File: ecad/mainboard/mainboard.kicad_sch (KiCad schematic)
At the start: 20 parts, among them J1 Dot Matrix Side A, J2 Dot Matrix Side B, J3 Dot Matrix Side A, J4 Dot Matrix Side B, J5 Conn_01x08_Socket, J6 Conn_01x08_Socket, J7 USB_C_Receptacle_PowerOnly_6P, J8 Conn_01x08_Socket, J9 Conn_01x08_Socket, SW1 Left Button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

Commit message: complete schematics for v1 of board
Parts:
- removed J7: USB_C_Receptacle_PowerOnly_6P, symbol Connector:USB_C_Receptacle_PowerOnly_6P
- added R10, R11, R12, R13, R14, R15, R16, R9: ${dm_resistor}, symbol Device:R_US
- added R17: 10k, symbol Device:R_US
- added R18, R19: 4.7k, symbol Device:R_US
- added U1: PCF8575DBR, Package_SO:SSOP-24_5.3x8.2mm_P0.65mm, symbol Interface_Expansion:PCF8575DBR
- J5: value Conn_01x08_Socket -> ESP32C3 Super Mini Left
- J6: value Conn_01x08_Socket -> ESP32C3 Super Mini Right
- J8: value Conn_01x08_Socket -> IO Expander Module - Left
- J9: value Conn_01x08_Socket -> IO Expander Module - Right
- R1, R2, R3, R4, R5, R6, R7, R8: value 330 -> ${dm_resistor}
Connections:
- net GPIO10 is gone; now on net BUZZ: J5.6 (Pin_6)
- net DM_A1: now also R1.1
- net DM_A2: now also R2.1
- net DM_A3: now also R3.1
- net DM_A4: now also R4.1
- net DM_A5: now also R5.1
- net DM_A6: now also R6.1
- net DM_A7: now also R7.1
- net DM_A8: now also R8.1
- net DM_B1: now also R9.1
- net DM_B2: now also R10.1
- net DM_B3: now also R11.1
- net DM_B4: now also R12.1
- net DM_B5: now also R13.1
- net DM_B6: now also R14.1
- net DM_B7: now also R15.1
- net DM_B8: now also R16.1
- net GND: now also U1.12 (GND), U1.2 (A1), U1.21 (A0), U1.3 (A2)
- net LEFT_BTN: now also J6.8 (Pin_8)
- net RIGHT_BTN: now also J6.7 (Pin_7)
- net SCL: now also R19.2, U1.22 (SCL)
- net SDA: now also R18.2, U1.23 (SDA)
- net P5: now reaches R6.2
- net P5: now also J8.6 (Pin_6), U1.9 (P5)
- net P4: now reaches R5.2
- net P4: now also J8.5 (Pin_5), U1.8 (P4)
- net P1: now reaches R2.2
- net P1: now also J8.2 (Pin_2), U1.5 (P1)
- net P0: now reaches R1.2
- net P0: now also J8.1 (Pin_1), U1.4 (P0)
- net P3: now reaches R4.2
- net P3: now also J8.4 (Pin_4), U1.7 (P3)
- net P7: now reaches R8.2
- net P7: now also J8.8 (Pin_8), U1.11 (P7)
- net P2: now reaches R3.2
- net P2: now also J8.3 (Pin_3), U1.6 (P2)
- net P6: now reaches J8.7 (Pin_7)
- net P6: now also R7.2, U1.10 (P6)
- net P10: now reaches J9.1 (Pin_1)
- net P10: now also R9.2, U1.13 (P10)
- net P11: now reaches J9.2 (Pin_2)
- net P11: now also R10.2, U1.14 (P11)
- net P12: now reaches J9.3 (Pin_3)
- net P12: now also R11.2, U1.15 (P12)
- net P13: now reaches J9.4 (Pin_4)
- net P13: now also R12.2, U1.16 (P13)
- net P14: now reaches J9.5 (Pin_5)
- net P14: now also R13.2, U1.17 (P14)
- net P15: now reaches J9.6 (Pin_6)
- net P15: now also R14.2, U1.18 (P15)
- net P16: now reaches J9.7 (Pin_7)
- net P16: now also R15.2, U1.19 (P16)
- net P17: now reaches J9.8 (Pin_8)
- net P17: now also R16.2, U1.20 (P17)
- net +5V: no longer names the net of J6.1 (Pin_1)
- net GPIO20: no longer names the net of J5.7 (Pin_7)
- net GPIO21: no longer names the net of J5.8 (Pin_8)
- removed net GPIO5: J5.1 (Pin_1), J6.3 (Pin_3), J6.4 (Pin_4), J6.5 (Pin_5), J6.6 (Pin_6), J6.7 (Pin_7), J6.8 (Pin_8)
- net GPIO6: no longer names the net of J5.2 (Pin_2)
- net GPIO7: no longer names the net of J5.3 (Pin_3)
- new net +3.3V: J6.3 (Pin_3), R17.1, R18.1, R19.1, U1.24 (VCC)
- new net ~{INT}: J6.5 (Pin_5), R17.2, U1.1 (~{INT})
- no-connect marks 0 -> 8
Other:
- moved on the sheet: BZ1, J1, J2, J3, J4, J5, J6, J8, J9, R1, R2, R3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

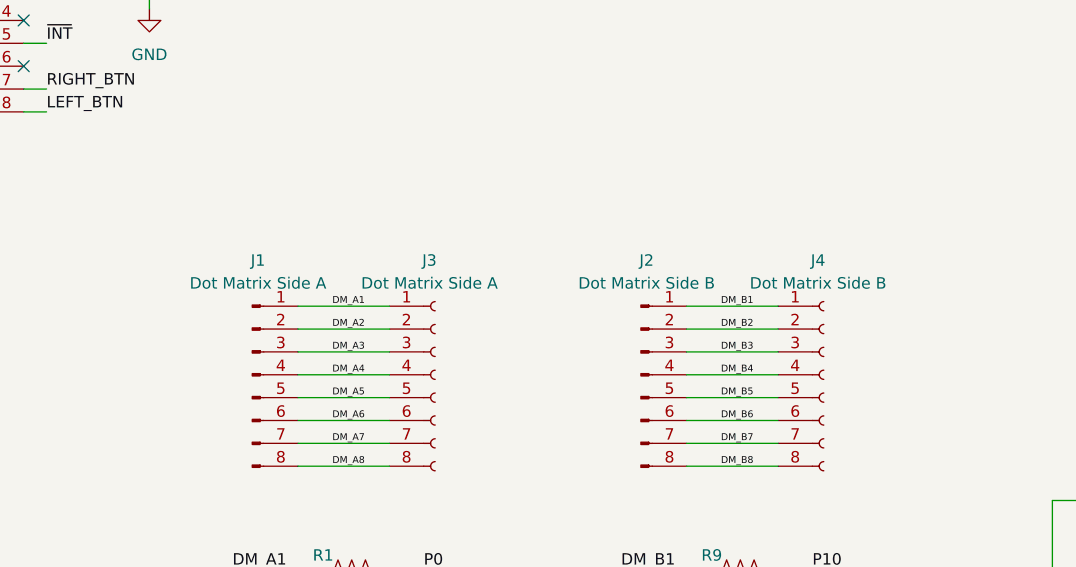
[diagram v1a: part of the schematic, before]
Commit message: update footprints for the schematic
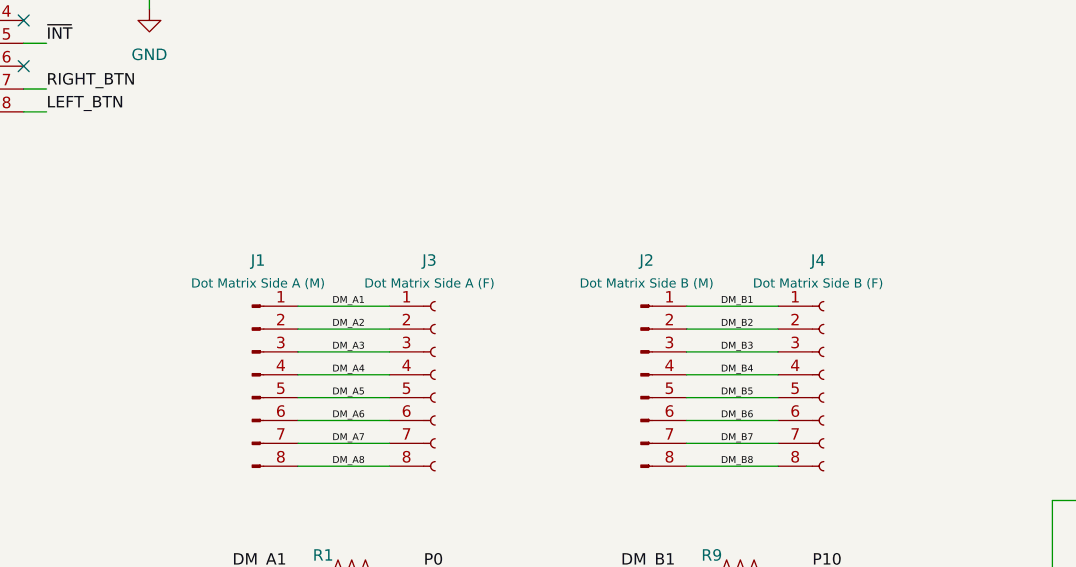
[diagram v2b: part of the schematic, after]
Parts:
- BZ1: footprint (none) -> Buzzer_Beeper:Buzzer_12x9.5RM7.6
- J1: value Dot Matrix Side A -> Dot Matrix Side A (M); footprint (none) -> Connector_PinHeader_2.54mm:PinHeader_1x08_P2.54mm_Vertical
- J2: value Dot Matrix Side B -> Dot Matrix Side B (M); footprint (none) -> Connector_PinHeader_2.54mm:PinHeader_1x08_P2.54mm_Vertical
- J3: value Dot Matrix Side A -> Dot Matrix Side A (F); footprint (none) -> Connector_PinSocket_2.54mm:PinSocket_1x08_P2.54mm_Vertical
- J4: value Dot Matrix Side B -> Dot Matrix Side B (F); footprint (none) -> Connector_PinSocket_2.54mm:PinSocket_1x08_P2.54mm_Vertical
- J5, J6, J8, J9: footprint (none) -> Connector_PinSocket_2.54mm:PinSocket_1x08_P2.54mm_Vertical
- R1, R10, R11, R12, R13, R14, R15, R16, R17, R18, R19, R2, R3, R4, R5, R6, R7, R8, R9: footprint (none) -> Resistor_SMD:R_0805_2012Metric
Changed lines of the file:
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@@
 			)
 		)
-		(property "Footprint" ""
+		(property "Footprint" "Resistor_SMD:R_0805_2012Metric"
 			(at 100.584 127.254 90)
 			(hide yes)
@@
 			)
 		)
-		(property "Value" "Dot Matrix Side B"
+		(property "Value" "Dot Matrix Side B (F)"
 			(at 151.765 64.77 0)
 			(show_name no)
@@
 			(effects
 				(font
-					(size 1.27 1.27)
+					(size 1.016 1.016)
 				)
 			)
 		)
-		(property "Footprint" ""
+		(property "Footprint" "Connector_PinSocket_2.54mm:PinSocket_1x08_P2.54mm_Vertical"
 			(at 152.4 74.93 0)
 			(hide yes)
@@
 			)
 		)
-		(property "Value" "Dot Matrix Side B"
+		(property "Value" "Dot Matrix Side B (M)"
 			(at 132.715 64.77 0)
 			(show_name no)
@@
 			(effects
 				(font
-					(size 1.27 1.27)
+					(size 1.016 1.016)
 				)
 			)
 		)
-		(property "Footprint" ""
+		(property "Footprint" "Connector_PinHeader_2.54mm:PinHeader_1x08_P2.54mm_Vertical"
 			(at 132.08 74.93 0)
 			(hide yes)
@@
 			)
 		)
-		(property "Footprint" ""
+		(property "Footprint" "Resistor_SMD:R_0805_2012Metric"
 			(at 100.584 120.904 90)
 			(hide yes)
@@
 			)
 		)
-		(property "Value" "Dot Matrix Side A"
+		(property "Value" "Dot Matrix Side A (F)"
 			(at 108.585 64.77 0)
 			(show_name no)
@@
 			(effects
 				(font
-					(size 1.27 1.27)
+					(size 1.016 1.016)
 				)
 			)
 		)
-		(property "Footprint" ""
+		(property "Footprint" "Connector_PinSocket_2.54mm:PinSocket_1x08_P2.54mm_Vertical"
 			(at 109.22 74.93 0)
 			(hide yes)
@@
 			)
 		)
-		(property "Footprint" ""
+		(property "Footprint" "Resistor_SMD:R_0805_2012Metric"
 			(at 143.764 141.224 90)
 			(hide yes)
@@
 			)
 		)
-		(property "Footprint" ""
+		(property "Footprint" "Resistor_SMD:R_0805_2012Metric"
 			(at 27.686 98.044 90)
 			(hide yes)
@@
 			)
 		)
-		(property "Footprint" ""
+		(property "Footprint" "Resistor_SMD:R_0805_2012Metric"
 			(at 143.764 114.554 90)
 			(hide yes)
@@
 			)
 		)
-		(property "Footprint" ""
+		(property "Footprint" "Resistor_SMD:R_0805_2012Metric"
 			(at 100.584 101.854 90)
 			(hide yes)
@@
 			)
 		)
-		(property "Footprint" ""
+		(property "Footprint" "Resistor_SMD:R_0805_2012Metric"
 			(at 100.584 95.504 90)
 			(hide yes)
@@
 			)
 		)
-		(property "Footprint" ""
+		(property "Footprint" "Resistor_SMD:R_0805_2012Metric"
 			(at 100.584 114.554 90)
 			(hide yes)
@@
 			)
 		)
-		(property "Footprint" ""
+		(property "Footprint" "Connector_PinSocket_2.54mm:PinSocket_1x08_P2.54mm_Vertical"
 			(at 27.94 35.56 0)
 			(hide yes)
@@
 			)
 		)
-		(property "Footprint" ""
+		(property "Footprint" "Resistor_SMD:R_0805_2012Metric"
 			(at 100.584 141.224 90)
 			(hide yes)
@@
 			)
 		)
-		(property "Footprint" ""
+		(property "Footprint" "Resistor_SMD:R_0805_2012Metric"
 			(at 143.764 133.604 90)
 			(hide yes)
@@
 			)
 		)
-		(property "Footprint" ""
+		(property "Footprint" "Resistor_SMD:R_0805_2012Metric"
 			(at 100.584 108.204 90)
 			(hide yes)
@@
 			)
 		)
-		(property "Value" "Dot Matrix Side A"
+		(property "Value" "Dot Matrix Side A (M)"
 			(at 89.535 64.77 0)
 			(show_name no)
@@
 			(effects
 				(font
-					(size 1.27 1.27)
+					(size 1.016 1.016)
 				)
 			)
 		)
-		(property "Footprint" ""
+		(property "Footprint" "Connector_PinHeader_2.54mm:PinHeader_1x08_P2.54mm_Vertical"
 			(at 88.9 74.93 0)
 			(hide yes)
@@
 			)
 		)
-		(property "Footprint" ""
+		(property "Footprint" "Resistor_SMD:R_0805_2012Metric"
 			(at 143.764 95.504 90)
 			(hide yes)
@@
 			)
 		)
-		(property "Footprint" ""
+		(property "Footprint" "Resistor_SMD:R_0805_2012Metric"
 			(at 39.116 98.044 90)
 			(hide yes)
@@
 			)
 		)
-		(property "Footprint" ""
+		(property "Footprint" "Connector_PinSocket_2.54mm:PinSocket_1x08_P2.54mm_Vertical"
 			(at 224.79 59.69 0)
 			(hide yes)
@@
 			)
 		)
-		(property "Footprint" ""
+		(property "Footprint" "Resistor_SMD:R_0805_2012Metric"
 			(at 143.764 108.204 90)
 			(hide yes)
@@
 			)
 		)
-		(property "Footprint" ""
+		(property "Footprint" "Resistor_SMD:R_0805_2012Metric"
 			(at 143.764 120.904 90)
 			(hide yes)
@@
 			)
 		)
-		(property "Footprint" ""
+		(property "Footprint" "Buzzer_Beeper:Buzzer_12x9.5RM7.6"
 			(at 26.035 170.18 90)
 			(hide yes)
@@
 			)
 		)
-		(property "Footprint" ""
+		(property "Footprint" "Connector_PinSocket_2.54mm:PinSocket_1x08_P2.54mm_Vertical"
 			(at 58.42 35.56 0)
 			(hide yes)
@@
 			)
 		)
-		(property "Footprint" ""
+		(property "Footprint" "Resistor_SMD:R_0805_2012Metric"
 			(at 178.816 108.204 90)
 			(hide yes)
@@
 			)
 		)
-		(property "Footprint" ""
+		(property "Footprint" "Resistor_SMD:R_0805_2012Metric"
 			(at 143.764 101.854 90)
 			(hide yes)
@@
 			)
 		)
-		(property "Footprint" ""
+		(property "Footprint" "Resistor_SMD:R_0805_2012Metric"
 			(at 100.584 133.604 90)
 			(hide yes)
@@
 			)
 		)
-		(property "Footprint" ""
+		(property "Footprint" "Resistor_SMD:R_0805_2012Metric"
 			(at 143.764 127.254 90)
 			(hide yes)
@@
 			)
 		)
-		(property "Footprint" ""
+		(property "Footprint" "Connector_PinSocket_2.54mm:PinSocket_1x08_P2.54mm_Vertical"
 			(at 260.35 59.69 0)
 			(hide yes)

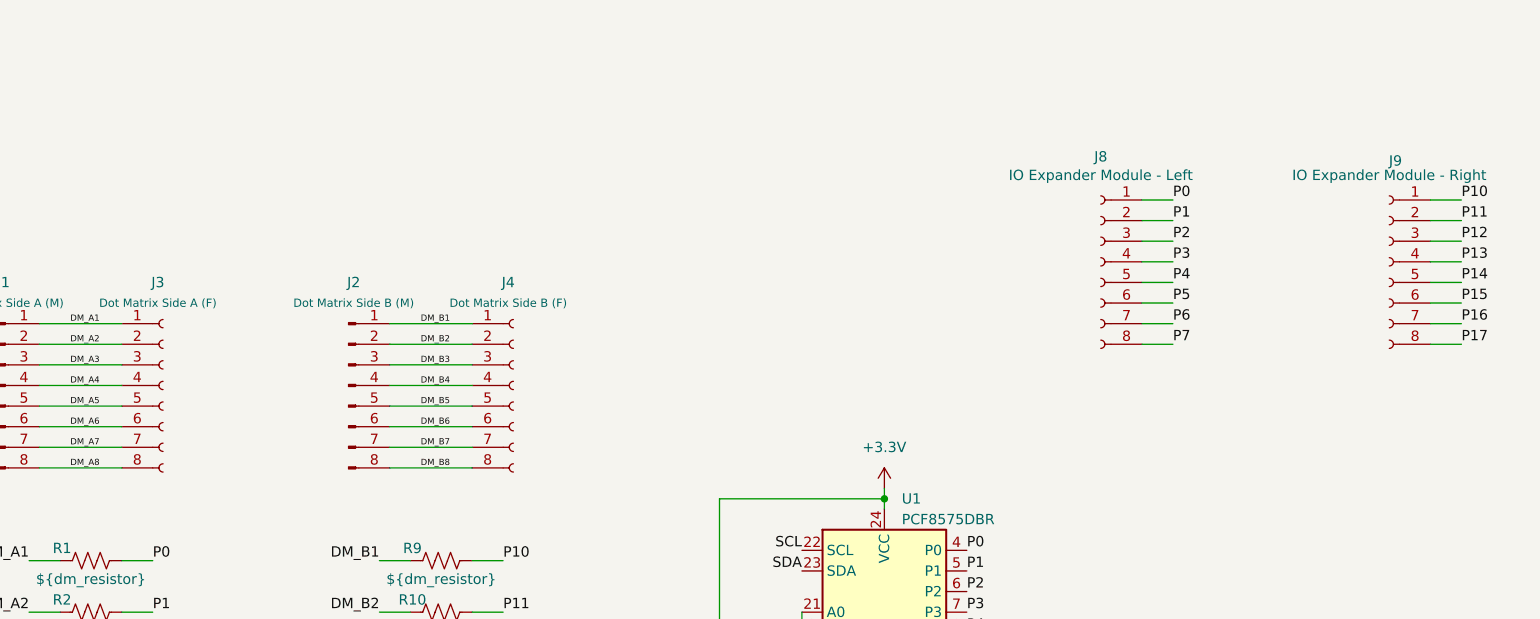
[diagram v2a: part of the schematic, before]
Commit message: update pin headers for dot matrix
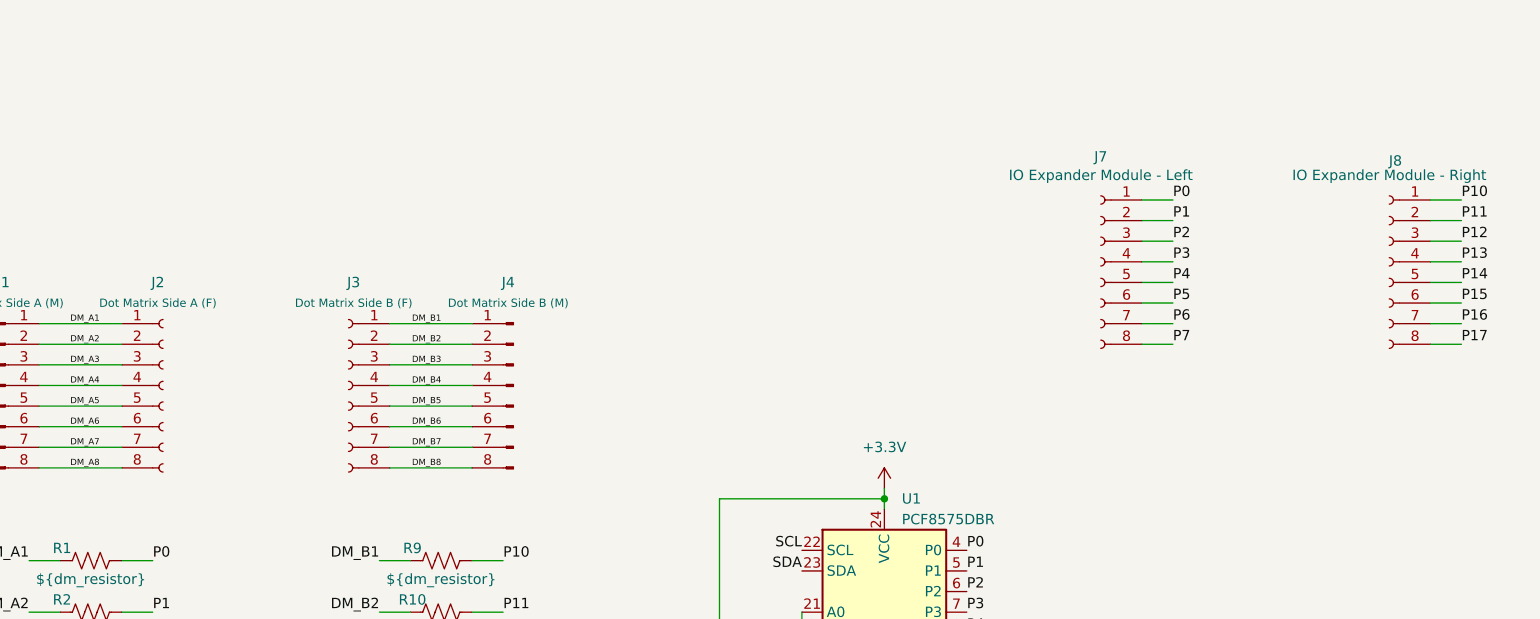
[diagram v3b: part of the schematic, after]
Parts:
- renumbered J3 to J2, J4 to J3, J2 to J4, J8 to J7, J9 to J8
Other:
- moved on the sheet: J3, J4
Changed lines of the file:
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@@
 	(wire
 		(pts
-			(xy 137.16 67.31) (xy 147.32 67.31)
+			(xy 147.32 67.31) (xy 137.16 67.31)
 		)
 		(stroke
@@
 	(wire
 		(pts
-			(xy 137.16 74.93) (xy 147.32 74.93)
+			(xy 147.32 74.93) (xy 137.16 74.93)
 		)
 		(stroke
@@
 	(wire
 		(pts
-			(xy 137.16 77.47) (xy 147.32 77.47)
+			(xy 147.32 77.47) (xy 137.16 77.47)
 		)
 		(stroke
@@
 	(wire
 		(pts
-			(xy 137.16 85.09) (xy 147.32 85.09)
+			(xy 147.32 85.09) (xy 137.16 85.09)
 		)
 		(stroke
@@
 	(wire
 		(pts
-			(xy 137.16 82.55) (xy 147.32 82.55)
+			(xy 147.32 82.55) (xy 137.16 82.55)
 		)
 		(stroke
@@
 	(wire
 		(pts
-			(xy 137.16 72.39) (xy 147.32 72.39)
+			(xy 147.32 72.39) (xy 137.16 72.39)
 		)
 		(stroke
@@
 	(wire
 		(pts
-			(xy 137.16 69.85) (xy 147.32 69.85)
+			(xy 147.32 69.85) (xy 137.16 69.85)
 		)
 		(stroke
@@
 	(wire
 		(pts
-			(xy 137.16 80.01) (xy 147.32 80.01)
+			(xy 147.32 80.01) (xy 137.16 80.01)
 		)
 		(stroke
@@
 	)
 	(label "DM_B2"
-		(at 140.97 69.85 0)
+		(at 143.51 69.85 180)
 		(effects
 			(font
 				(size 0.762 0.762)
 			)
-			(justify left bottom)
+			(justify right bottom)
 		)
 	)
@@
 	)
 	(label "DM_B6"
-		(at 140.97 80.01 0)
+		(at 143.51 80.01 180)
 		(effects
 			(font
 				(size 0.762 0.762)
 			)
-			(justify left bottom)
+			(justify right bottom)
 		)
 	)
 	(label "DM_B8"
-		(at 140.97 85.09 0)
+		(at 143.51 85.09 180)
 		(effects
 			(font
 				(size 0.762 0.762)
 			)
-			(justify left bottom)
+			(justify right bottom)
 		)
 	)
@@
 	)
 	(label "DM_B3"
-		(at 140.97 72.39 0)
+		(at 143.51 72.39 180)
 		(effects
 			(font
 				(size 0.762 0.762)
 			)
-			(justify left bottom)
+			(justify right bottom)
 		)
 	)
@@
 	)
 	(label "DM_B4"
-		(at 140.97 74.93 0)
+		(at 143.51 74.93 180)
 		(effects
 			(font
 				(size 0.762 0.762)
 			)
-			(justify left bottom)
+			(justify right bottom)
 		)
 	)
@@
 	)
 	(label "DM_B1"
-		(at 140.97 67.31 0)
+		(at 143.51 67.31 180)
 		(effects
 			(font
 				(size 0.762 0.762)
 			)
-			(justify left bottom)
+			(justify right bottom)
 		)
 	)
@@
 	)
 	(label "DM_B7"
-		(at 140.97 82.55 0)
+		(at 143.51 82.55 180)
 		(effects
 			(font
 				(size 0.762 0.762)
 			)
-			(justify left bottom)
+			(justify right bottom)
 		)
 	)
@@
 	)
 	(label "DM_B5"
-		(at 140.97 77.47 0)
+		(at 143.51 77.47 180)
 		(effects
 			(font
 				(size 0.762 0.762)
 			)
-			(justify left bottom)
+			(justify right bottom)
 		)
 	)
@@
 	(symbol
 		(lib_id "Connector:Conn_01x08_Socket")
-		(at 152.4 74.93 0)
+		(at 132.08 74.93 0)
+		(mirror y)
 		(unit 1)
 		(body_style 1)
@@
 		(in_pos_files yes)
 		(dnp no)
-		(property "Reference" "J4"
-			(at 151.765 62.23 0)
+		(property "Reference" "J3"
+			(at 132.715 62.23 0)
 			(show_name no)
 			(do_not_autoplace no)
@@
 		)
 		(property "Value" "Dot Matrix Side B (F)"
-			(at 151.765 64.77 0)
+			(at 132.715 64.77 0)
 			(show_name no)
 			(do_not_autoplace no)
@@
 		)
 		(property "Footprint" "Connector_PinSocket_2.54mm:PinSocket_1x08_P2.54mm_Vertical"
-			(at 152.4 74.93 0)
+			(at 132.08 74.93 0)
 			(hide yes)
 			(show_name no)
@@
 		)
 		(property "Datasheet" ""
-			(at 152.4 74.93 0)
+			(at 132.08 74.93 0)
 			(hide yes)
 			(show_name no)
@@
 		)
 		(property "Description" "Generic connector, single row, 01x08, script generated"
-			(at 152.4 74.93 0)
+			(at 132.08 74.93 0)
 			(hide yes)
 			(show_name no)
@@
 			(project "mainboard"
 				(path "/daa70da3-6ce4-4871-9367-b401b0239362"
-					(reference "J4")
+					(reference "J3")
 					(unit 1)
 				)
@@
 	(symbol
 		(lib_id "Connector:Conn_01x08_Pin")
-		(at 132.08 74.93 0)
+		(at 152.4 74.93 0)
+		(mirror y)
 		(unit 1)
 		(body_style 1)
@@
 		(dnp no)
 		(fields_autoplaced yes)
-		(property "Reference" "J2"
-			(at 132.715 62.23 0)
+		(property "Reference" "J4"
+			(at 151.765 62.23 0)
 			(show_name no)
 			(do_not_autoplace no)
@@
 		)
 		(property "Value" "Dot Matrix Side B (M)"
-			(at 132.715 64.77 0)
+			(at 151.765 64.77 0)
 			(show_name no)
 			(do_not_autoplace no)
@@
 		)
 		(property "Footprint" "Connector_PinHeader_2.54mm:PinHeader_1x08_P2.54mm_Vertical"
-			(at 132.08 74.93 0)
+			(at 152.4 74.93 0)
 			(hide yes)
 			(show_name no)
@@
 		)
 		(property "Datasheet" ""
-			(at 132.08 74.93 0)
+			(at 152.4 74.93 0)
 			(hide yes)
 			(show_name no)
@@
 		)
 		(property "Description" "Generic connector, single row, 01x08, script generated"
-			(at 132.08 74.93 0)
+			(at 152.4 74.93 0)
 			(hide yes)
 			(show_name no)
@@
 			(project "mainboard"
 				(path "/daa70da3-6ce4-4871-9367-b401b0239362"
-					(reference "J2")
+					(reference "J4")
 					(unit 1)
 				)
@@
 		(in_pos_files yes)
 		(dnp no)
-		(property "Reference" "J3"
+		(property "Reference" "J2"
 			(at 108.585 62.23 0)
 			(show_name no)
@@
 			(project "mainboard"
 				(path "/daa70da3-6ce4-4871-9367-b401b0239362"
-					(reference "J3")
+					(reference "J2")
 					(unit 1)
 				)
@@
 		(in_pos_files yes)
 		(dnp no)
-		(property "Reference" "J8"
+		(property "Reference" "J7"
 			(at 224.79 46.736 0)
 			(show_name no)
@@
 			(project "mainboard"
 				(path "/daa70da3-6ce4-4871-9367-b401b0239362"
-					(reference "J8")
+					(reference "J7")
 					(unit 1)
 				)
@@
 		(in_pos_files yes)
 		(dnp no)
-		(property "Reference" "J9"
+		(property "Reference" "J8"
 			(at 261.112 47.244 0)
 			(show_name no)
@@
 			(project "mainboard"
 				(path "/daa70da3-6ce4-4871-9367-b401b0239362"
-					(reference "J9")
+					(reference "J8")
 					(unit 1)
 				)
